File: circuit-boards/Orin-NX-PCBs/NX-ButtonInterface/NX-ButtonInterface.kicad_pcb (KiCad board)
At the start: 2 copper layers, 48.3 x 16.8 mm, 3 parts, among them J1 NX CONTROL & UART, J2 CAN-NX, J3 NX-BUTTON

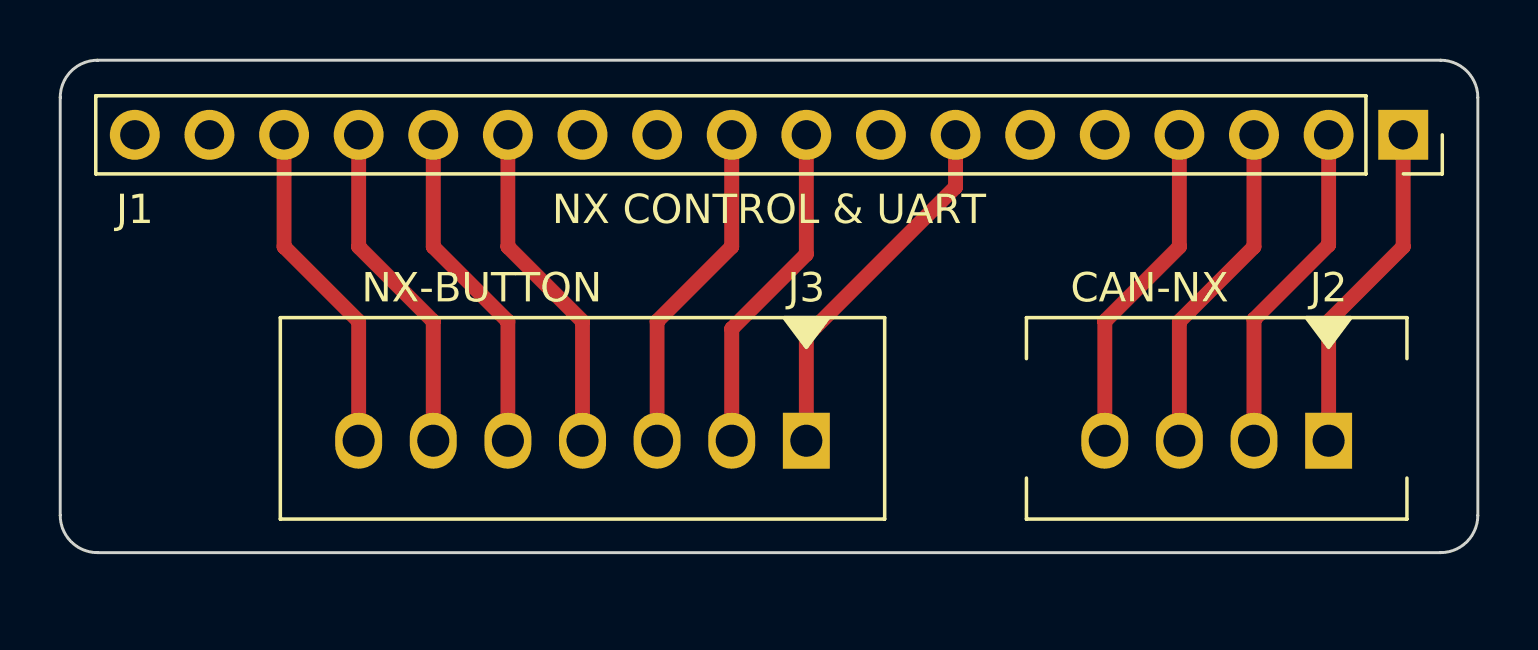
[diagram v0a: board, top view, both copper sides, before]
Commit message: Change SL connectors to surface mount solder wires.
Signed-off-by: Scott Berman <sgberman1@gmail.com>
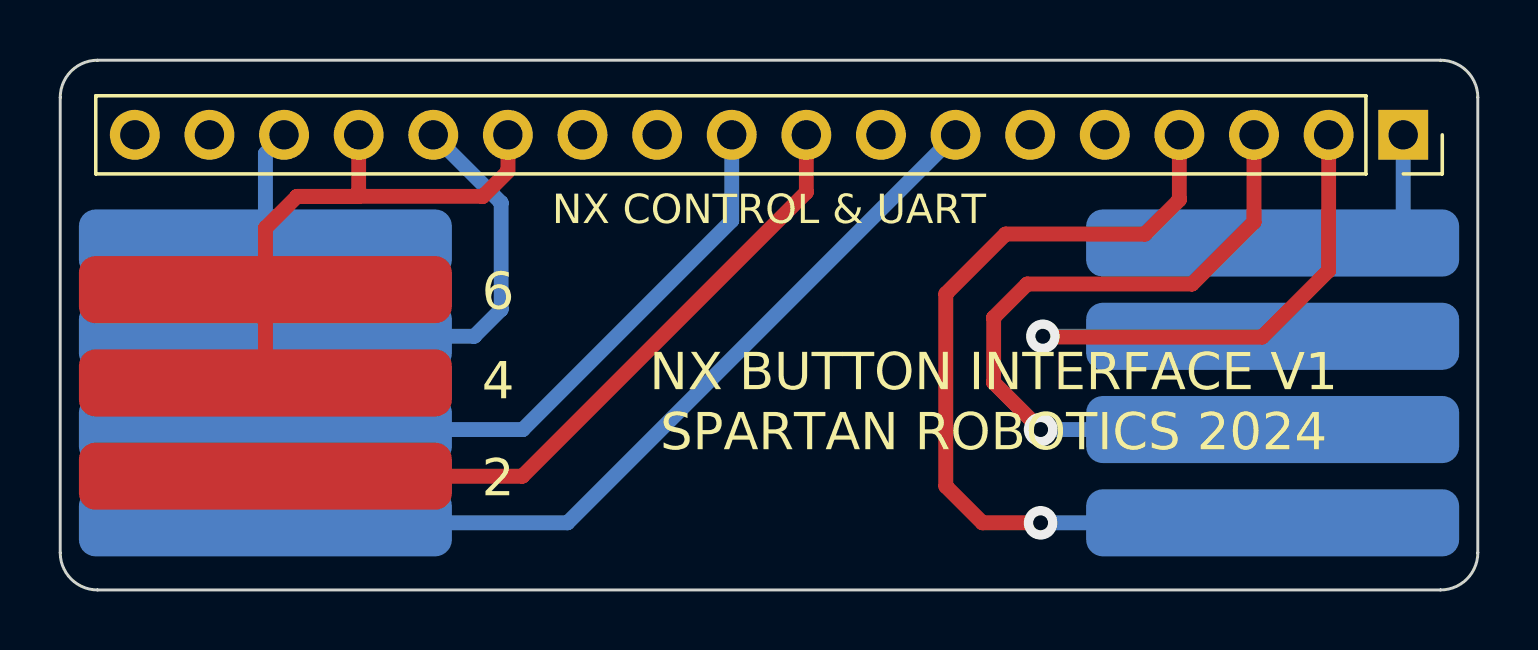
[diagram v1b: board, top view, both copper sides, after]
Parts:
- J2: footprint NX-ButtonInterface:70543-0003 -> NX-ButtonInterface:4-pin-solder-pads; moved to B.Cu
- J3: footprint NX-ButtonInterface:70543-0006 -> NX-ButtonInterface:7-pin-solder-pads; moved to B.Cu
- moved J3 19.6 mm to (91.2, 96.6), turned to 180 degrees
- moved J2 3.38 mm to (125.5, 106.2)
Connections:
- J2 pad 1: /CAN_TX -> /3V3
- J2 pad 2: /CAN_RX -> /GND
- J2 pad 3: /GND -> /CAN_RX
- J2 pad 4: /3V3 -> /CAN_TX
- J3 pad 1: /NX_PC_LED- -> /~{REC}
- J3 pad 2: /UART2_RXD -> /SYS_RST_RCV_RTN
- J3 pad 3: /UART2_TXD -> /~{SYS_RESET}
- J3 pad 5: /~{SYS_RESET} -> /UART2_TXD
- J3 pad 6: /SYS_RST_RCV_RTN -> /UART2_RXD
- J3 pad 7: /~{REC} -> /NX_PC_LED-
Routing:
- net /3V3: track 11.5 -> 29.7 mm, vias 0 -> 1
- net /NX_PC_LED-: track 12.5 -> 29.0 mm
- net /GND: track 11.5 -> 25.6 mm, vias 0 -> 1
- net /UART2_RXD: track 11.5 -> 24.4 mm
- net /CAN_RX: track 11.5 -> 23.1 mm, vias 0 -> 1
- net /UART2_TXD: track 11.5 -> 21.7 mm
- net /~{REC}: track 11.5 -> 3.95 mm
- net /~{SYS_RESET}: track 11.5 -> 15.3 mm
- net /CAN_TX: track 11.5 -> 8.13 mm
- net /SYS_RST_RCV_RTN: track 22.9 -> 19.8 mm
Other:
- board size 48.3 x 16.8 mm -> 48.3 x 18 mm
- board text added: "1"
- board text added: "2"
- board text added: "3"
- board text added: "4"
- board text added: "5"
- board text added: "6"
- board text added: "7"
